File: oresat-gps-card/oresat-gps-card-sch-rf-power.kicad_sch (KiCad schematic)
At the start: 25 parts, among them U15 SKY65723-81, U16 BP2G+, U17 MAX8510EXK29+T, U18 MAX8510EXK29+T, U19 MAX8510EXK33+T

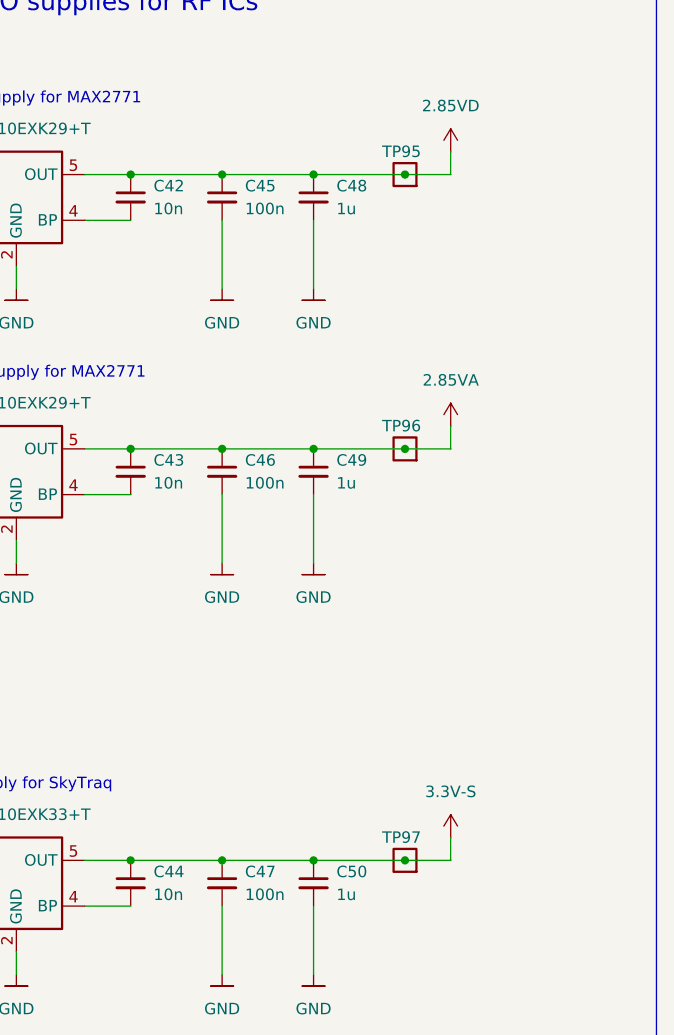
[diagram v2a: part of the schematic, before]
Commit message: Updated GPS card with changes from C3 and notes. Fixed library issues
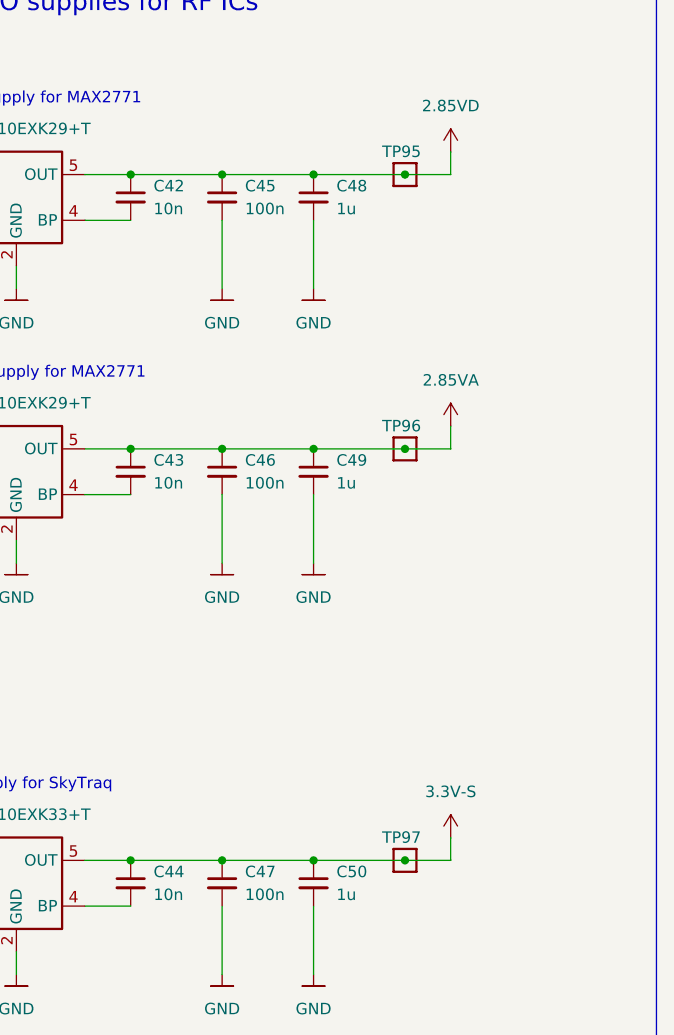
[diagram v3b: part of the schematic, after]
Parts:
- TP95, TP96, TP97: value Test-Point -> 0.03x0.04; footprint OreSat-TestPoint:PAD.03X.04 -> oresat-misc:TestPoint_Pad_D1.0mm; symbol OreSat-TestPoint:Test-Point -> oresat-misc:Test-Point-1mm-round
- U15: symbol U-Skyworks-SKY65723-81-gps-low-noise-amplifier-front-end:SKY65723-81 -> oresat-ics:SKY65723-81
- U16: symbol U-Minicircuits-BP2G+l-band-splitter:BP2G+ -> oresat-ics:BP2G+
- U17, U18, U19: symbol U-Maxim-MAX8510EXK29+T-low-noise-LDO-2v85:MAX8510EXK29+T -> oresat-ics:MAX8510EXK29+T

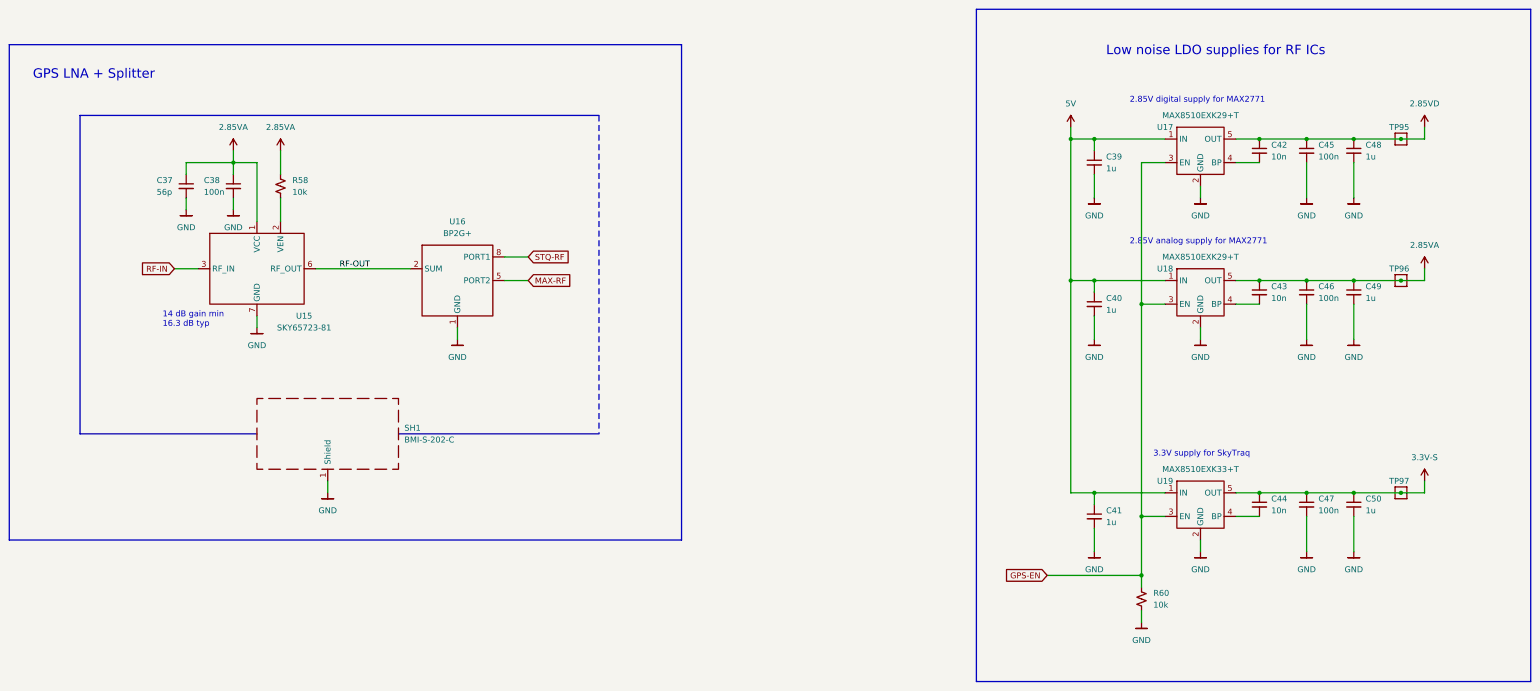
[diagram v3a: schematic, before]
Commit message: Updated GPS card
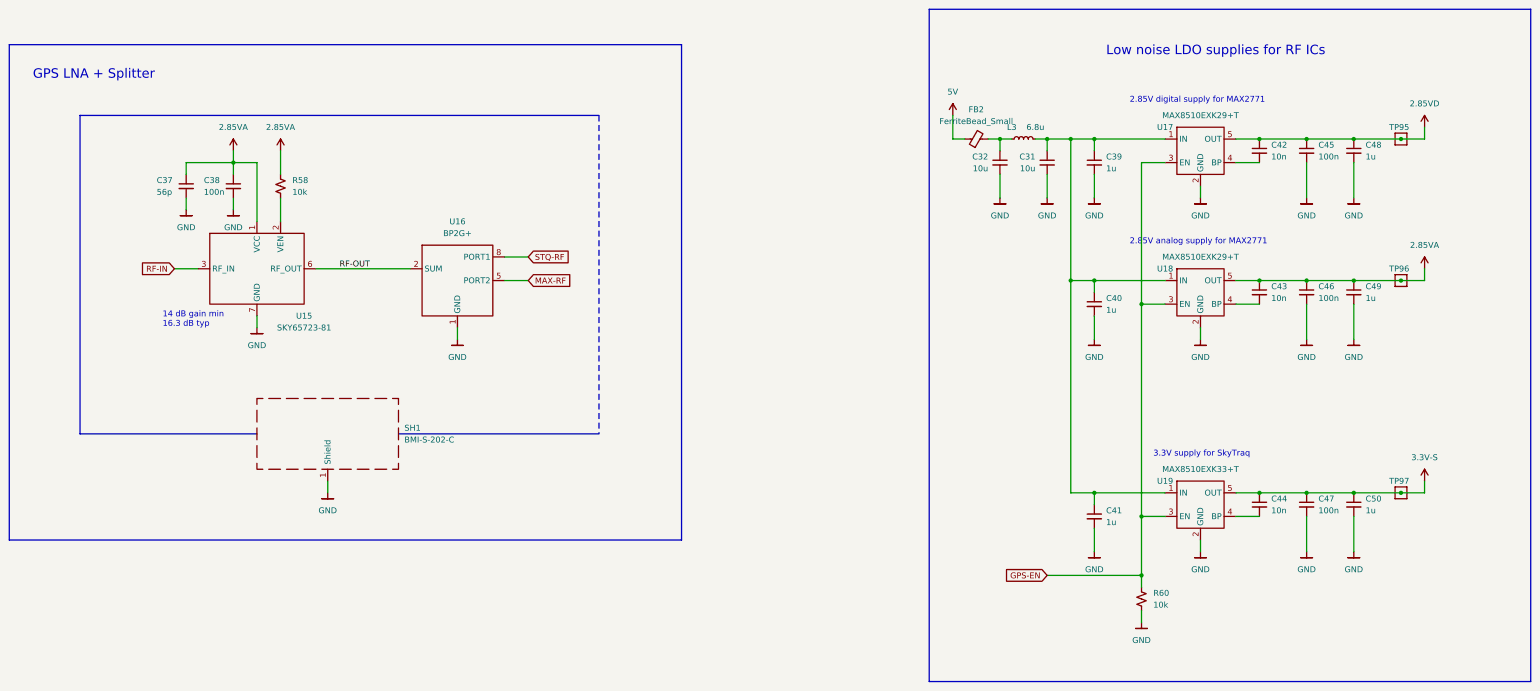
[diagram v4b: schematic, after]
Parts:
- added C31, C32: 10u, Capacitor_SMD:C_0805_2012Metric, symbol Device:C_Small
- added FB2: FerriteBead_Small, Resistor_SMD:R_0805_2012Metric, symbol Device:FerriteBead_Small
- added L3: 6.8u, oresat-passives:L_ECS-MPI4040, symbol Device:L_Small
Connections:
- net 5V: now also FB2.1; no longer C39.1, C40.1, C41.1, U17.1 (IN), U18.1 (IN), U19.1 (IN)
- net GND: now also C31.2, C32.2
- new net: C31.1, C39.1, C40.1, C41.1, L3.2, U17.1 (IN), U18.1 (IN), U19.1 (IN)
- new net: C32.1, FB2.2, L3.1
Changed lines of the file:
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@@
   (junction (at 289.56 109.22) (diameter 0) (color 0 0 0 0)
   )
+  (junction (at 259.08 73.66) (diameter 0) (color 0 0 0 0)
+  )
   (junction (at 279.4 73.66) (diameter 0) (color 0 0 0 0)
   )
@@
   (junction (at 325.12 73.66) (diameter 0) (color 0 0 0 0)
   )
+  (junction (at 269.24 73.66) (diameter 0) (color 0 0 0 0)
+  )
   (junction (at 289.56 154.94) (diameter 0) (color 0 0 0 0)
   )
@@
     (stroke (width 0) (type default))
   )
-  (wire (pts (xy 274.32 73.66) (xy 274.32 71.12))
-    (stroke (width 0) (type default))
-  )
   (wire (pts (xy 93.98 76.2) (xy 93.98 78.74))
     (stroke (width 0) (type default))
@@
     (stroke (width 0) (type default))
   )
+  (wire (pts (xy 269.24 81.28) (xy 269.24 86.36))
+    (stroke (width 0) (type default))
+  )
   (polyline (pts (xy 129.54 137.16) (xy 172.72 137.16))
     (stroke (width 0) (type default))
@@
     (stroke (width 0) (type default))
   )
+  (wire (pts (xy 259.08 81.28) (xy 259.08 86.36))
+    (stroke (width 0) (type default))
+  )
   (wire (pts (xy 335.28 73.66) (xy 345.44 73.66))
     (stroke (width 0) (type default))
@@
     (stroke (width 0) (type default))
   )
+  (wire (pts (xy 269.24 73.66) (xy 274.32 73.66))
+    (stroke (width 0) (type default))
+  )
   (polyline (pts (xy 60.96 68.58) (xy 172.72 68.58))
     (stroke (width 0) (type default))
@@
     (stroke (width 0) (type default))
   )
+  (wire (pts (xy 259.08 73.66) (xy 261.62 73.66))
+    (stroke (width 0) (type default))
+  )
   (wire (pts (xy 279.4 149.86) (xy 274.32 149.86))
     (stroke (width 0) (type default))
@@
     (stroke (width 0) (type default))
   )
-  (polyline (pts (xy 254 190.5) (xy 373.38 190.5))
+  (polyline (pts (xy 243.84 190.5) (xy 373.38 190.5))
     (stroke (width 0) (type default))
   )
@@
     (stroke (width 0) (type default))
   )
-  (polyline (pts (xy 373.38 45.72) (xy 254 45.72))
+  (polyline (pts (xy 373.38 45.72) (xy 243.84 45.72))
+    (stroke (width 0) (type default))
+  )
+  (wire (pts (xy 259.08 76.2) (xy 259.08 73.66))
     (stroke (width 0) (type default))
   )
@@
     (stroke (width 0) (type default))
   )
-  (polyline (pts (xy 254 45.72) (xy 254 190.5))
+  (polyline (pts (xy 243.84 45.72) (xy 243.84 190.5))
     (stroke (width 0) (type default))
   )
@@
     (stroke (width 0) (type default))
   )
+  (wire (pts (xy 269.24 76.2) (xy 269.24 73.66))
+    (stroke (width 0) (type default))
+  )
   (wire (pts (xy 279.4 152.4) (xy 279.4 149.86))
     (stroke (width 0) (type default))
@@
     (stroke (width 0) (type default))
   )
+  (wire (pts (xy 259.08 73.66) (xy 256.54 73.66))
+    (stroke (width 0) (type default))
+  )
   (wire (pts (xy 279.4 106.68) (xy 279.4 104.14))
     (stroke (width 0) (type default))
@@
     (stroke (width 0) (type default))
   )
+  (wire (pts (xy 248.92 73.66) (xy 251.46 73.66))
+    (stroke (width 0) (type default))
+  )
   (wire (pts (xy 302.26 160.02) (xy 302.26 162.56))
     (stroke (width 0) (type default))
@@
     (stroke (width 0) (type default))
   )
+  (wire (pts (xy 269.24 73.66) (xy 266.7 73.66))
+    (stroke (width 0) (type default))
+  )
   (wire (pts (xy 289.56 175.26) (xy 289.56 177.8))
     (stroke (width 0) (type default))
@@
   )
   (wire (pts (xy 335.28 149.86) (xy 345.44 149.86))
+    (stroke (width 0) (type default))
+  )
+  (wire (pts (xy 248.92 68.58) (xy 248.92 73.66))
     (stroke (width 0) (type default))
   )
@@
     )
   )
+  (symbol (lib_id "oresat-power:GND") (at 269.24 86.36 0) (unit 1)
+    (in_bom yes) (on_board yes) (dnp no)
+    (property "Reference" "#GND02" (at 269.24 92.71 0)
+      (effects (font (size 1.27 1.27)) hide)
+    )
+    (property "Value" "GND" (at 269.24 90.17 0)
+      (effects (font (size 1.27 1.27)))
+    )
+    (property "Footprint" "" (at 269.24 86.36 0)
+      (effects (font (size 1.27 1.27)) hide)
+    )
+    (property "Datasheet" "" (at 269.24 86.36 0)
+      (effects (font (size 1.27 1.27)) hide)
+    )
+    (pin "1")
+    (instances
+      (project "oresat-gps-card"
+        (path "/65d12cdd-c326-4033-9053-c59fa4e0b25e/9466b485-4fbd-4df7-9d49-44799fc3f2b8"
+          (reference "#GND02") (unit 1)
+        )
+      )
+    )
+  )
   (symbol (lib_id "gps-power:2.85VA") (at 93.98 76.2 0) (unit 1)
     (in_bom no) (on_board no) (dnp no) (fields_autoplaced)
@@
     )
   )
+  (symbol (lib_id "oresat-power:GND") (at 259.08 86.36 0) (unit 1)
+    (in_bom yes) (on_board yes) (dnp no)
+    (property "Reference" "#GND03" (at 259.08 92.71 0)
+      (effects (font (size 1.27 1.27)) hide)
+    )
+    (property "Value" "GND" (at 259.08 90.17 0)
+      (effects (font (size 1.27 1.27)))
+    )
+    (property "Footprint" "" (at 259.08 86.36 0)
+      (effects (font (size 1.27 1.27)) hide)
+    )
+    (property "Datasheet" "" (at 259.08 86.36 0)
+      (effects (font (size 1.27 1.27)) hide)
+    )
+    (pin "1")
+    (instances
+      (project "oresat-gps-card"
+        (path "/65d12cdd-c326-4033-9053-c59fa4e0b25e/9466b485-4fbd-4df7-9d49-44799fc3f2b8"
+          (reference "#GND03") (unit 1)
+        )
+      )
+    )
+  )
   (symbol (lib_id "oresat-power:GND") (at 114.3 149.86 0) (unit 1)
     (in_bom yes) (on_board yes) (dnp no) (fields_autoplaced)
@@
         (path "/65d12cdd-c326-4033-9053-c59fa4e0b25e/9466b485-4fbd-4df7-9d49-44799fc3f2b8"
           (reference "#GND0190") (unit 1)
+        )
+      )
+    )
+  )
+  (symbol (lib_id "Device:FerriteBead_Small") (at 254 73.66 90) (unit 1)
+    (in_bom yes) (on_board yes) (dnp no) (fields_autoplaced)
+    (property "Reference" "FB2" (at 253.9619 67.31 90)
+      (effects (font (size 1.27 1.27)))
+    )
+    (property "Value" "FerriteBead_Small" (at 253.9619 69.85 90)
+      (effects (font (size 1.27 1.27)))
+    )
+    (property "Footprint" "Resistor_SMD:R_0805_2012Metric" (at 254 75.438 90)
+      (effects (font (size 1.27 1.27)) hide)
+    )
+    (property "Datasheet" "~" (at 254 73.66 0)
+      (effects (font (size 1.27 1.27)) hide)
+    )
+    (pin "1")
+    (pin "2")
+    (instances
+      (project "oresat-gps-card"
+        (path "/65d12cdd-c326-4033-9053-c59fa4e0b25e/9466b485-4fbd-4df7-9d49-44799fc3f2b8"
+          (reference "FB2") (unit 1)
         )
       )
@@
     )
   )
+  (symbol (lib_id "Device:L_Small") (at 264.16 73.66 90) (unit 1)
+    (in_bom yes) (on_board yes) (dnp no)
+    (property "Reference" "L3" (at 261.62 71.12 90)
+      (effects (font (size 1.27 1.27)))
+    )
+    (property "Value" "6.8u" (at 266.7 71.12 90)
+      (effects (font (size 1.27 1.27)))
+    )
+    (property "Footprint" "oresat-passives:L_ECS-MPI4040" (at 264.16 73.66 0)
+      (effects (font (size 1.27 1.27)) hide)
+    )
+    (property "Datasheet" "~" (at 264.16 73.66 0)
+      (effects (font (size 1.27 1.27)) hide)
+    )
+    (pin "1")
+    (pin "2")
+    (instances
+      (project "oresat-gps-card"
+        (path "/65d12cdd-c326-4033-9053-c59fa4e0b25e/9466b485-4fbd-4df7-9d49-44799fc3f2b8"
+          (reference "L3") (unit 1)
+        )
+      )
+    )
+  )
   (symbol (lib_id "gps-power:2.85VA") (at 350.52 101.6 0) (unit 1)
     (in_bom no) (on_board no) (dnp no) (fields_autoplaced)
@@
     )
   )
+  (symbol (lib_id "Device:C_Small") (at 259.08 78.74 0) (mirror y) (unit 1)
+    (in_bom yes) (on_board yes) (dnp no)
+    (property "Reference" "C32" (at 256.54 77.4762 0)
+      (effects (font (size 1.27 1.27)) (justify left))
+    )
+    (property "Value" "10u" (at 256.54 80.0162 0)
+      (effects (font (size 1.27 1.27)) (justify left))
+    )
+    (property "Footprint" "Capacitor_SMD:C_0805_2012Metric" (at 259.08 78.74 0)
+      (effects (font (size 1.27 1.27)) hide)
+    )
+    (property "Datasheet" "~" (at 259.08 78.74 0)
+      (effects (font (size 1.27 1.27)) hide)
+    )
+    (pin "1")
+    (pin "2")
+    (instances
+      (project "oresat-gps-card"
+        (path "/65d12cdd-c326-4033-9053-c59fa4e0b25e/9466b485-4fbd-4df7-9d49-44799fc3f2b8"
+          (reference "C32") (unit 1)
+        )
+      )
+    )
+  )
   (symbol (lib_id "oresat-misc:Test-Point-1mm-round") (at 345.44 104.14 180) (unit 1)
     (in_bom yes) (on_board yes) (dnp no)
@@
     )
   )
-  (symbol (lib_id "oresat-power:5V") (at 274.32 71.12 0) (unit 1)
-    (in_bom yes) (on_board yes) (dnp no)
-    (property "Reference" "#5V0104" (at 274.32 74.93 0)
-      (effects (font (size 1.27 1.27)) hide)
-    )
-    (property "Value" "5V" (at 274.32 66.04 0)
-      (effects (font (size 1.27 1.27)))
-    )
-    (property "Footprint" "" (at 274.32 71.12 0)
-      (effects (font (size 1.27 1.27)) hide)
-    )
-    (property "Datasheet" "" (at 274.32 71.12 0)
+  (symbol (lib_id "oresat-power:5V") (at 248.92 68.58 0) (unit 1)
+    (in_bom yes) (on_board yes) (dnp no)
+    (property "Reference" "#5V0104" (at 248.92 72.39 0)
+      (effects (font (size 1.27 1.27)) hide)
+    )
+    (property "Value" "5V" (at 248.92 63.5 0)
+      (effects (font (size 1.27 1.27)))
+    )
+    (property "Footprint" "" (at 248.92 68.58 0)
+      (effects (font (size 1.27 1.27)) hide)
+    )
+    (property "Datasheet" "" (at 248.92 68.58 0)
       (effects (font (size 1.27 1.27)) hide)
     )
@@
         )
       )
+    )
+  )
+  (symbol (lib_id "Device:C_Small") (at 269.24 78.74 0) (mirror y) (unit 1)
+    (in_bom yes) (on_board yes) (dnp no)
+    (property "Reference" "C31" (at 266.7 77.4762 0)
+      (effects (font (size 1.27 1.27)) (justify left))
+    )
+    (property "Value" "10u" (at 266.7 80.0162 0)
+      (effects (font (size 1.27 1.27)) (justify left))
+    )
+    (property "Footprint" "Capacitor_SMD:C_0805_2012Metric" (at 269.24 78.74 0)
+      (effects (font (size 1.27 1.27)) hide)
+    )
+    (property "Datasheet" "~" (at 269.24 78.74 0)
+      (effects (font (size 1.27 1.27)) hide)
+    )
+    (pin "1")
+    (pin "2")
+    (instances
+      (project "oresat-gps-card"
+        (path "/65d12cdd-c326-4033-9053-c59fa4e0b25e/9466b485-4fbd-4df7-9d49-44799fc3f2b8"
+          (reference "C31") (unit 1)
+        )
+      )

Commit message: Cleaned up ERC and DRC errors on GPS card
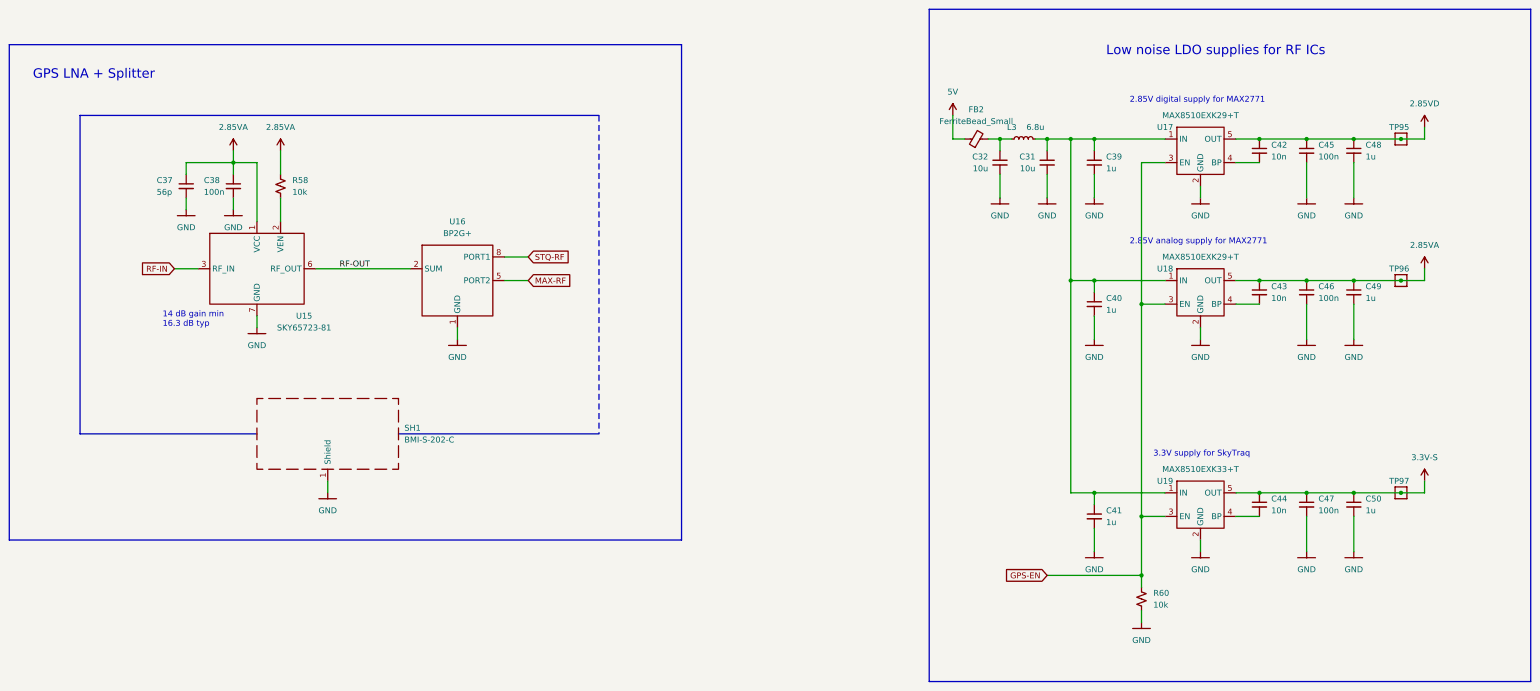
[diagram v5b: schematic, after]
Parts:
- U15: footprint oresat-footprints:U-Skyworks-SKY65723-81-gps-lna -> oresat-ics:U-Skyworks-SKY65723-81-gps-lna
- U16: footprint oresat-footprints:U-Minicircuits-BP2G+ -> oresat-ics:U-Minicircuits-BP2G+
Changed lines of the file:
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@@
       (effects (font (size 1.27 1.27)))
     )
-    (property "Footprint" "oresat-footprints:U-Minicircuits-BP2G+" (at 143.51 93.98 0)
+    (property "Footprint" "oresat-ics:U-Minicircuits-BP2G+" (at 143.51 93.98 0)
       (effects (font (size 1.27 1.27)) hide)
     )
@@
       (effects (font (size 1.27 1.27)))
     )
-    (property "Footprint" "oresat-footprints:U-Skyworks-SKY65723-81-gps-lna" (at 96.52 88.9 0)
-      (effects (font (size 1.27 1.27)) hide)
-    )
+    (property "Footprint" "oresat-ics:U-Skyworks-SKY65723-81-gps-lna" (at 96.52 88.9 0)
+      (effects (font (size 1.27 1.27)) hide)
+    )

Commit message: Updated KiCAD 8, updated schematic sheet info, polished some schematic things, and made DNP parts DNP.
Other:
- title: (none) -> OreSat GPS Card
